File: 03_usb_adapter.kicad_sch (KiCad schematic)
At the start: 5 parts

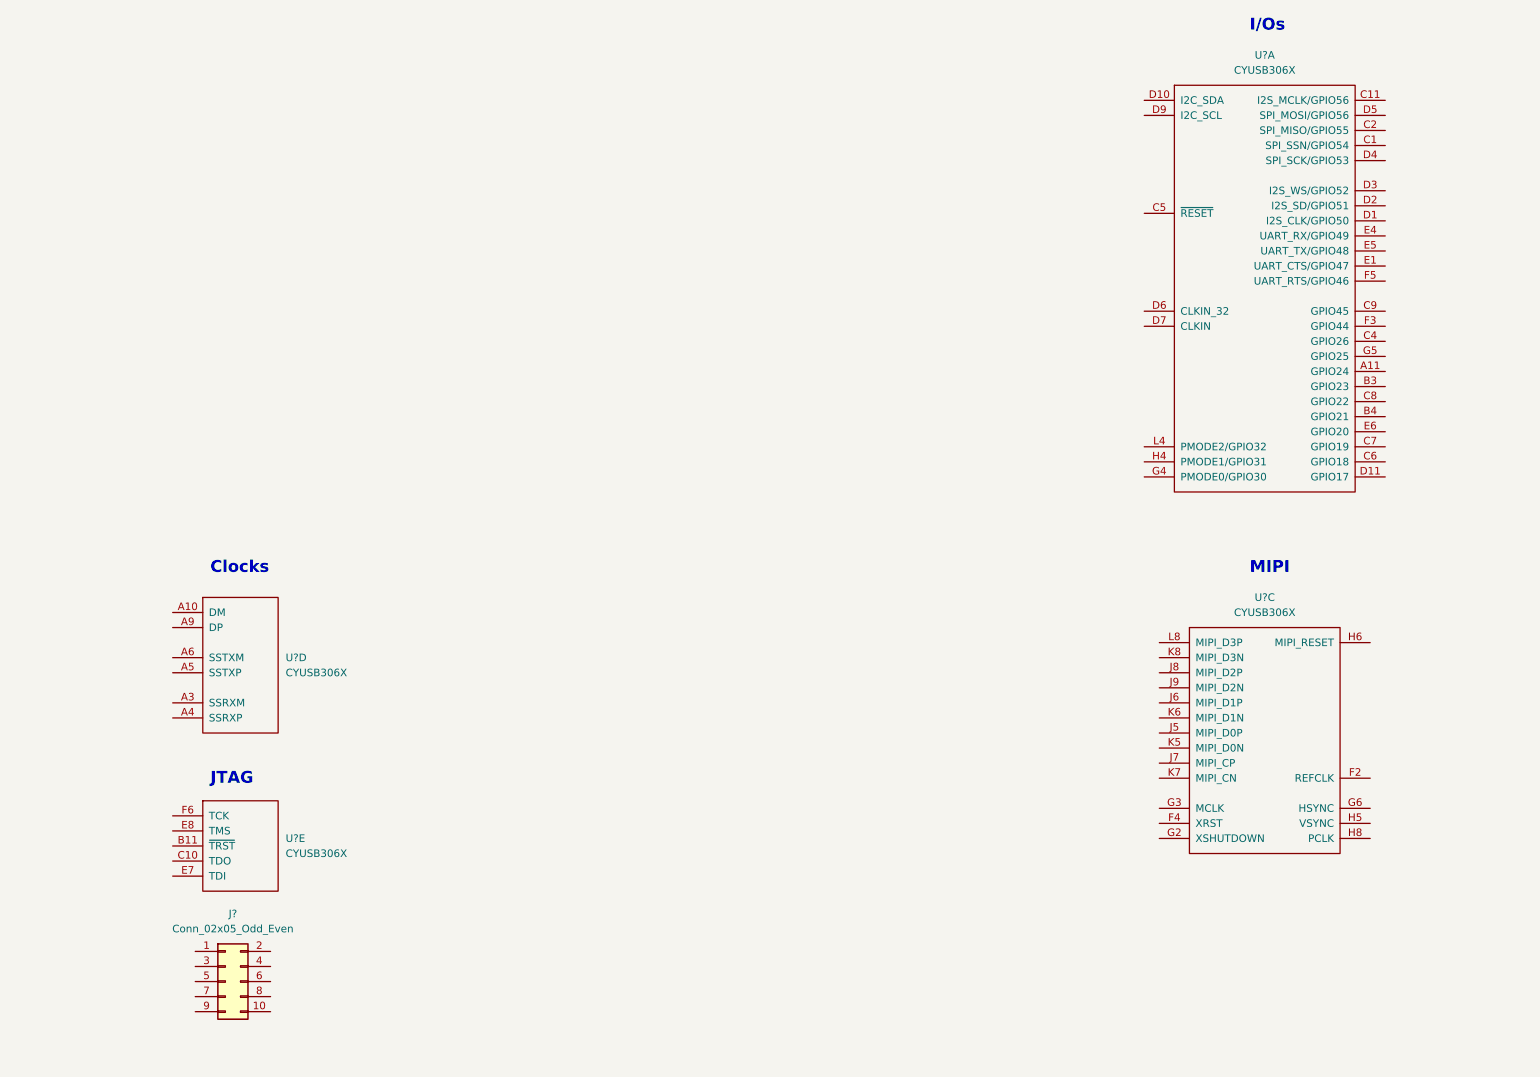
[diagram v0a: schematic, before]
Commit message: finished usb interface and added some new components
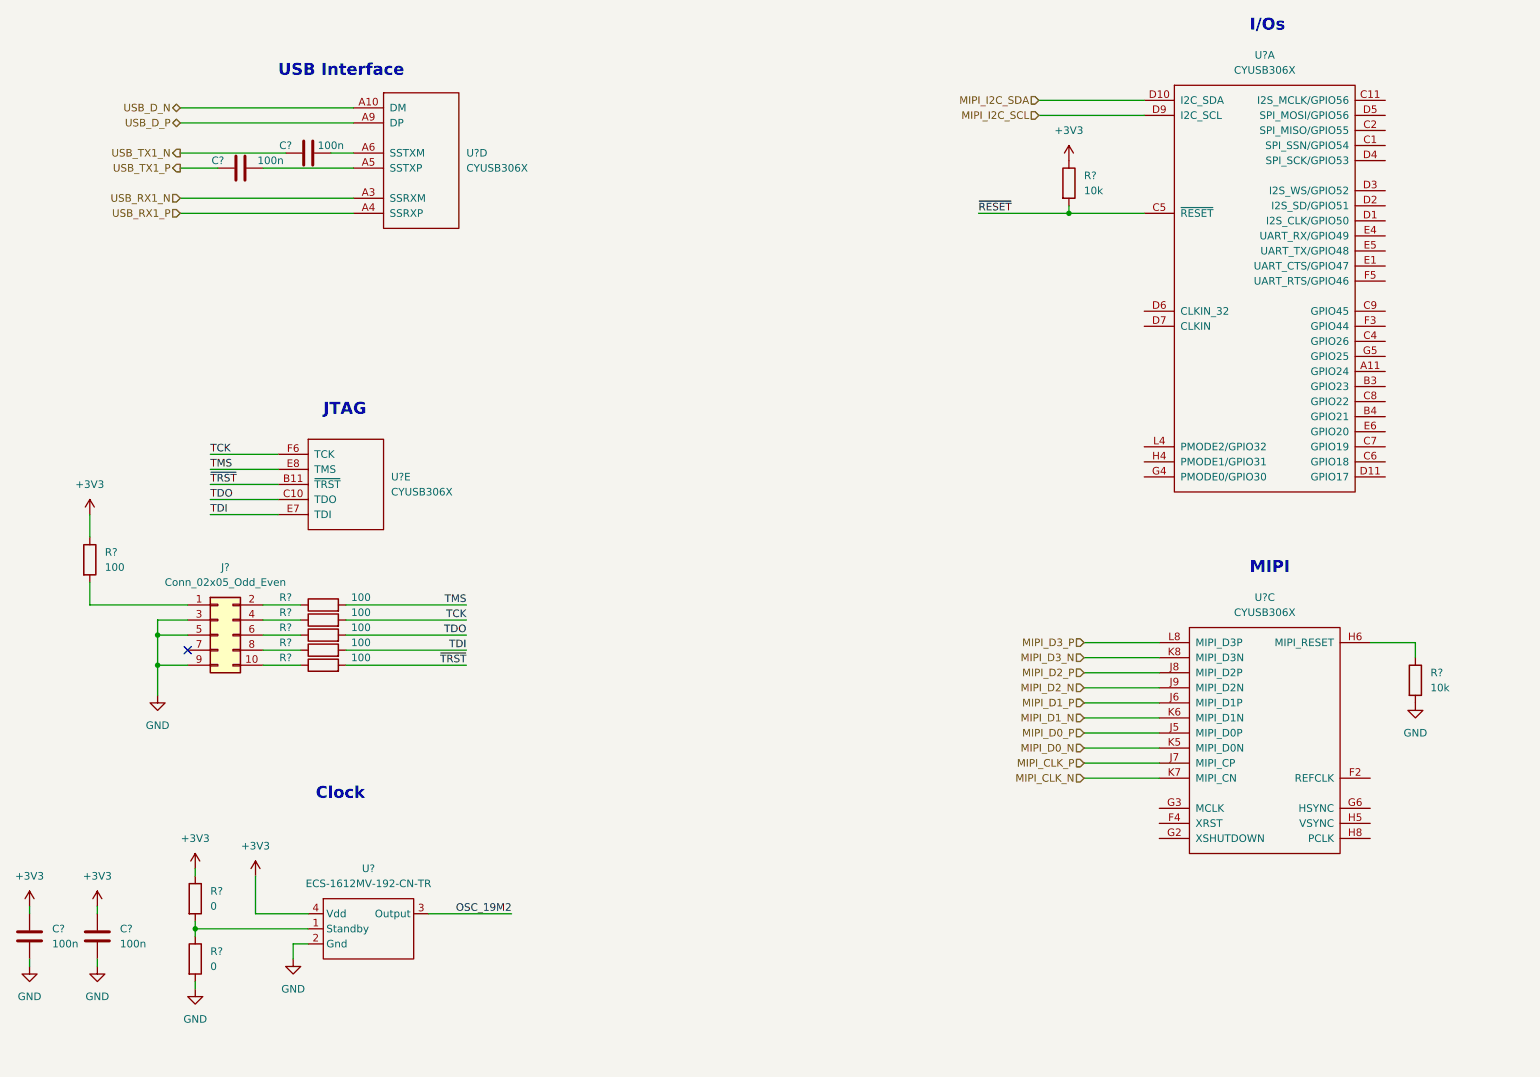
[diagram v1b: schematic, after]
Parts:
- added C? (x2): 100n, Capacitor_SMD:C_0603_1608Metric, symbol Device:C
- added C? (x2): 100n, symbol Device:C
- added R? (x2): 10k, Resistor_SMD:R_0603_1608Metric, symbol Device:R
- added R? (x2): 0, Resistor_SMD:R_0603_1608Metric, symbol Device:R
- added R? (x6): 100, Resistor_SMD:R_0603_1608Metric, symbol Device:R
- added U?: ECS-1612MV-192-CN-TR, samaritan:Crystal_SMD_ECS_1.6x1.2, symbol samaritan:ECS-1612MV-192-CN-TR
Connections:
- net at J?.1 (Pin_1): now also R?.2
- net at J?.10 (Pin_10): now also R?.1
- net at J?.2 (Pin_2): now also R?.1
- net GND: now reaches J?.3 (Pin_3)
- net GND: now also J?.5 (Pin_5), J?.9 (Pin_9), C?.2, C?.2, R?.2, R?.2, U?.2 (Gnd)
- net at J?.4 (Pin_4): now also R?.1
- net at J?.6 (Pin_6): now also R?.1
- net at J?.8 (Pin_8): now also R?.1
- net at U?.H6 (MIPI_RESET): now also R?.1
- net MIPI_D0_P: now reaches U?.J5 (MIPI_D0P)
- net MIPI_D1_P: now reaches U?.J6 (MIPI_D1P)
- net MIPI_CLK_P: now reaches U?.J7 (MIPI_CP)
- net MIPI_D2_P: now reaches U?.J8 (MIPI_D2P)
- net MIPI_D2_N: now reaches U?.J9 (MIPI_D2N)
- net MIPI_D0_N: now reaches U?.K5 (MIPI_D0N)
- net MIPI_D1_N: now reaches U?.K6 (MIPI_D1N)
- net MIPI_CLK_N: now reaches U?.K7 (MIPI_CN)
- net MIPI_D3_N: now reaches U?.K8 (MIPI_D3N)
- net MIPI_D3_P: now reaches U?.L8 (MIPI_D3P)
- net ~{RESET}: now reaches U?.C5 (~{RESET})
- net ~{RESET}: now also R?.2
- net MIPI_I2C_SDA: now reaches U?.D10 (I2C_SDA)
- net MIPI_I2C_SCL: now reaches U?.D9 (I2C_SCL)
- net ~{TRST}: now reaches U?.B11 (~{TRST})
- net ~{TRST}: now also R?.2
- net TDO: now reaches U?.C10 (TDO)
- net TDO: now also R?.2
- net TDI: now reaches U?.E7 (TDI)
- net TDI: now also R?.2
- net TMS: now reaches U?.E8 (TMS)
- net TMS: now also R?.2
- net TCK: now reaches U?.F6 (TCK)
- net TCK: now also R?.2
- net USB_D_N: now reaches U?.A10 (DM)
- net USB_RX1_N: now reaches U?.A3 (SSRXM)
- net USB_RX1_P: now reaches U?.A4 (SSRXP)
- net at U?.A5 (SSTXP): now also C?.2
- net at U?.A6 (SSTXM): now also C?.2
- net USB_D_P: now reaches U?.A9 (DP)
- new net: R?.1, R?.2, U?.1 (Standby)
- new net +3V3: C?.1, C?.1, R?.1, R?.1, R?.1, U?.4 (Vdd)
- new net OSC_19M2: U?.3 (Output)
- new net USB_TX1_N: C?.1
- new net USB_TX1_P: C?.1
- no-connect marks 0 -> 1
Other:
- note added: "Clock"
- note added: "USB Interface"
- note removed: "Clocks"
- moved on the sheet: J?, U?D, U?E

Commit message: added mipi connector
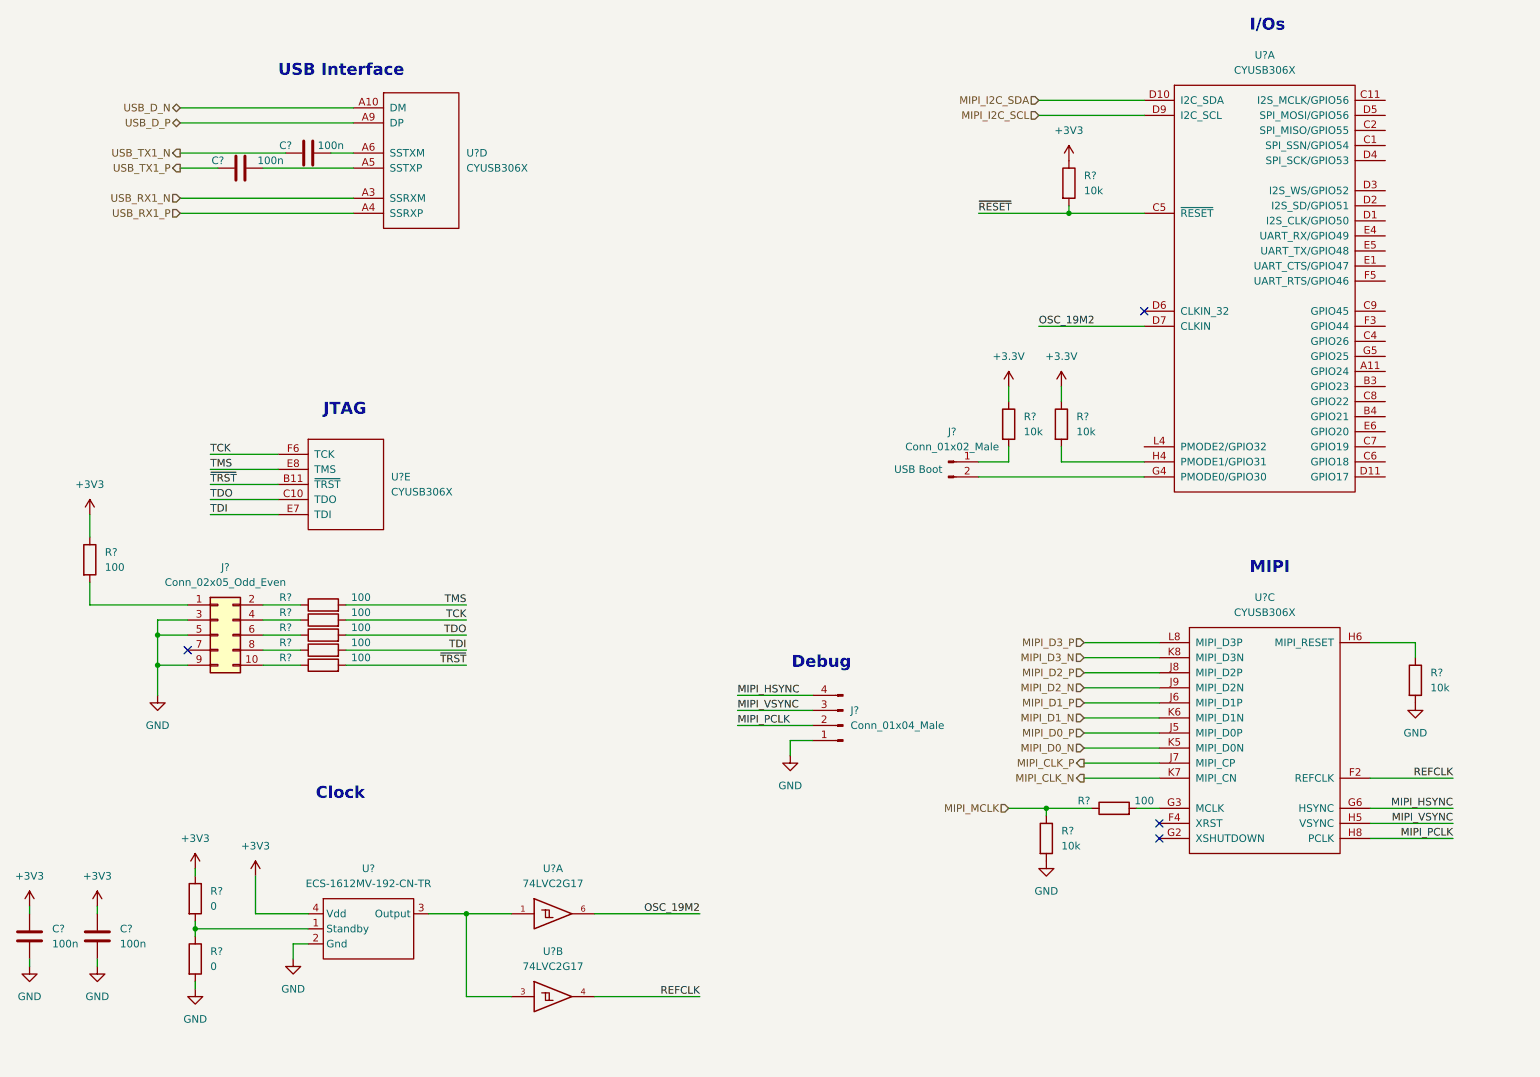
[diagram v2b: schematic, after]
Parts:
- added J?: Conn_01x04_Male, Connector_PinHeader_2.00mm:PinHeader_1x04_P2.00mm_Vertical, symbol Connector:Conn_01x04_Male
- added J?: Conn_01x02_Male, symbol Connector:Conn_01x02_Male
- added R? (x3): 10k, Resistor_SMD:R_0603_1608Metric, symbol Device:R
- added R?: 100, Resistor_SMD:R_0603_1608Metric, symbol Device:R
- added U? (x2): 74LVC2G17, symbol 74xGxx:74LVC2G17
- J?: footprint (none) -> Connector_PinHeader_2.00mm:PinHeader_2x05_P2.00mm_Vertical
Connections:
- net GND: now also J?.1 (Pin_1), R?.2, U?.2 (GND), U?.2 (GND)
- net OSC_19M2: now also U?.D7 (CLKIN), U?.6; no longer U?.3 (Output)
- net REFCLK: now reaches U?.F2 (REFCLK)
- net REFCLK: now also U?.4
- net at U?.G3 (MCLK): now also R?.2
- net MIPI_HSYNC: now reaches U?.G6 (HSYNC)
- net MIPI_HSYNC: now also J?.4 (Pin_4)
- net MIPI_VSYNC: now reaches U?.H5 (VSYNC)
- net MIPI_VSYNC: now also J?.3 (Pin_3)
- net MIPI_PCLK: now reaches U?.H8 (PCLK)
- net MIPI_PCLK: now also J?.2 (Pin_2)
- net at U?.G4 (PMODE0/GPIO30): now also J?.2 (Pin_2)
- net at U?.H4 (PMODE1/GPIO31): now also R?.2
- new net: U?.1, U?.3, U?.3 (Output)
- new net: J?.1 (Pin_1), R?.2
- new net +3.3V: R?.1, R?.1
- new net MIPI_MCLK: R?.1, R?.1
- new net VCC: U?.5 (VCC), U?.5 (VCC)
- no-connect marks 1 -> 4
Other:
- note added: "Debug"

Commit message: finished first pass of the schematics
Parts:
- U?: footprint (none) -> Package_BGA:TFBGA-121_10x10mm_Layout11x11_P0.8mm
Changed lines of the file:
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@@
     (effects (font (size 1.27 1.27)) (justify right))
   )
-  (hierarchical_label "MIPI_I2C_SCL" (shape input) (at 195.58 34.29 180)
+  (hierarchical_label "MIPI_I2C_SCL" (shape output) (at 195.58 34.29 180)
     (effects (font (size 1.27 1.27)) (justify right))
   )
@@
     (effects (font (size 1.27 1.27)) (justify right))
   )
-  (hierarchical_label "MIPI_I2C_SDA" (shape input) (at 195.58 31.75 180)
+  (hierarchical_label "MIPI_I2C_SDA" (shape bidirectional) (at 195.58 31.75 180)
     (effects (font (size 1.27 1.27)) (justify right))
   )
@@
     (effects (font (size 1.27 1.27)) (justify right))
   )
-  (hierarchical_label "MIPI_MCLK" (shape input) (at 190.5 151.13 180)
+  (hierarchical_label "MIPI_MCLK" (shape output) (at 190.5 151.13 180)
     (effects (font (size 1.27 1.27)) (justify right))
   )
@@
     (property "Reference" "U?" (id 0) (at 233.68 24.13 0))
     (property "Value" "CYUSB306X" (id 1) (at 233.68 26.67 0))
-    (property "Footprint" "" (id 2) (at 242.57 92.71 0)
-      (effects (font (size 1.27 1.27)) hide)
-    )
+    (property "Footprint" "Package_BGA:TFBGA-121_10x10mm_Layout11x11_P0.8mm" (id 2) (at 242.57 92.71 0)
+      (effects (font (size 1.27 1.27)) hide)
+    )

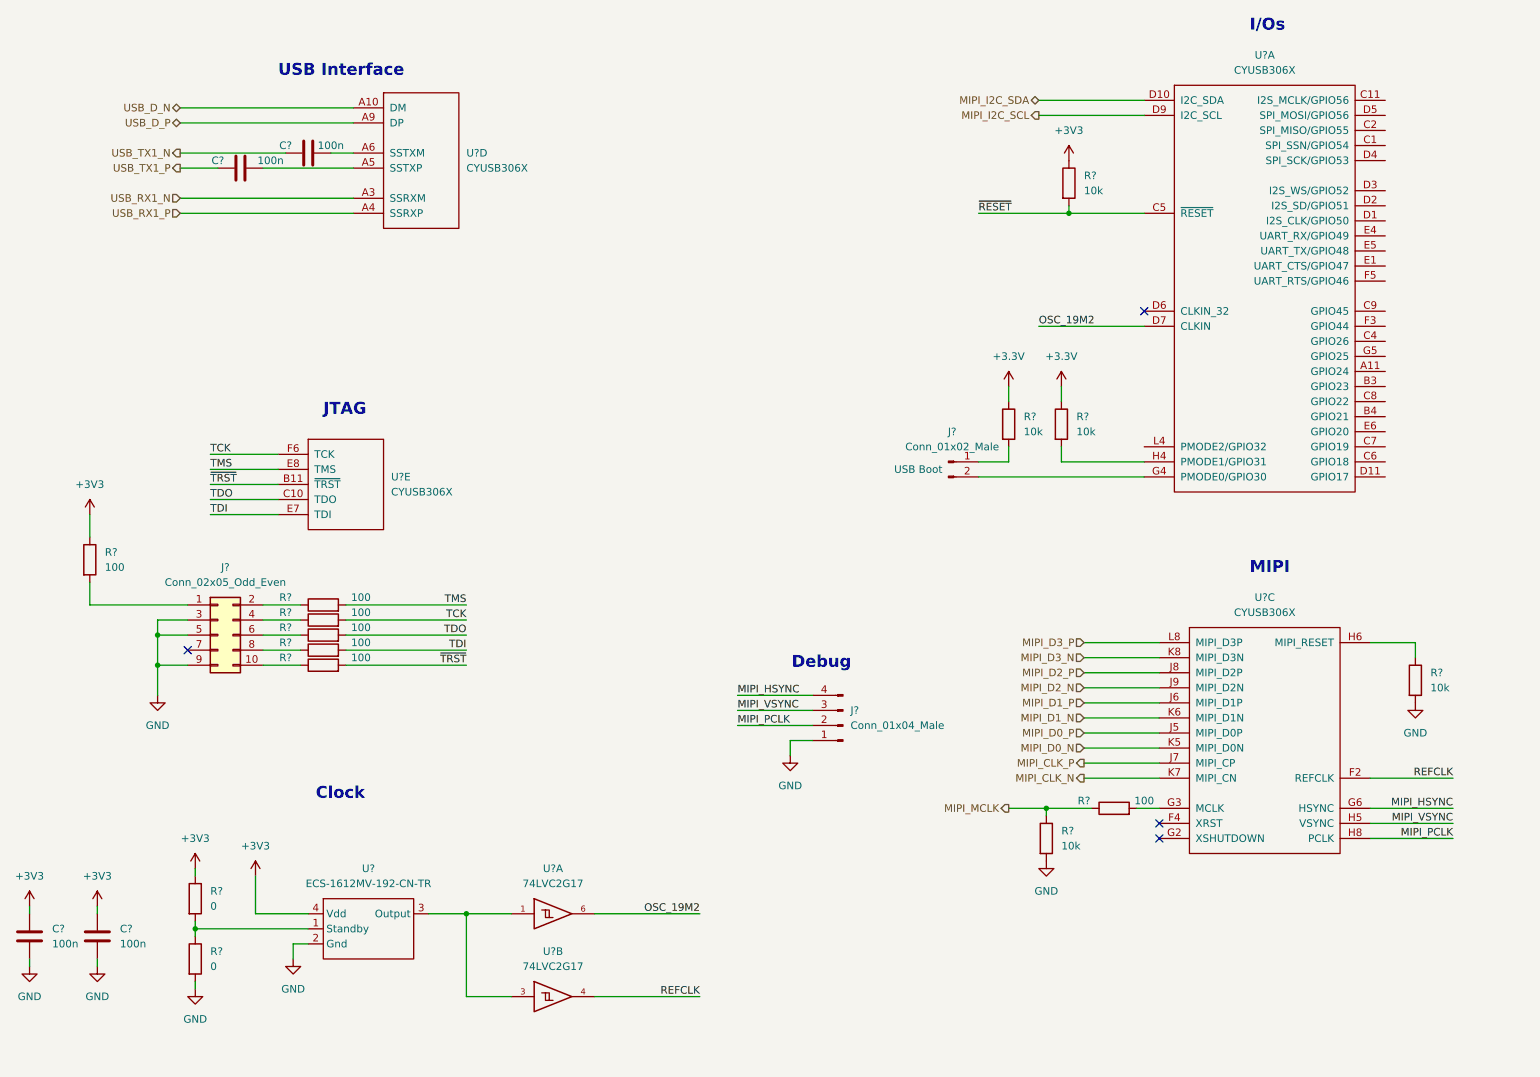
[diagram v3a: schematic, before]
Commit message: cleaned up some DRC errors
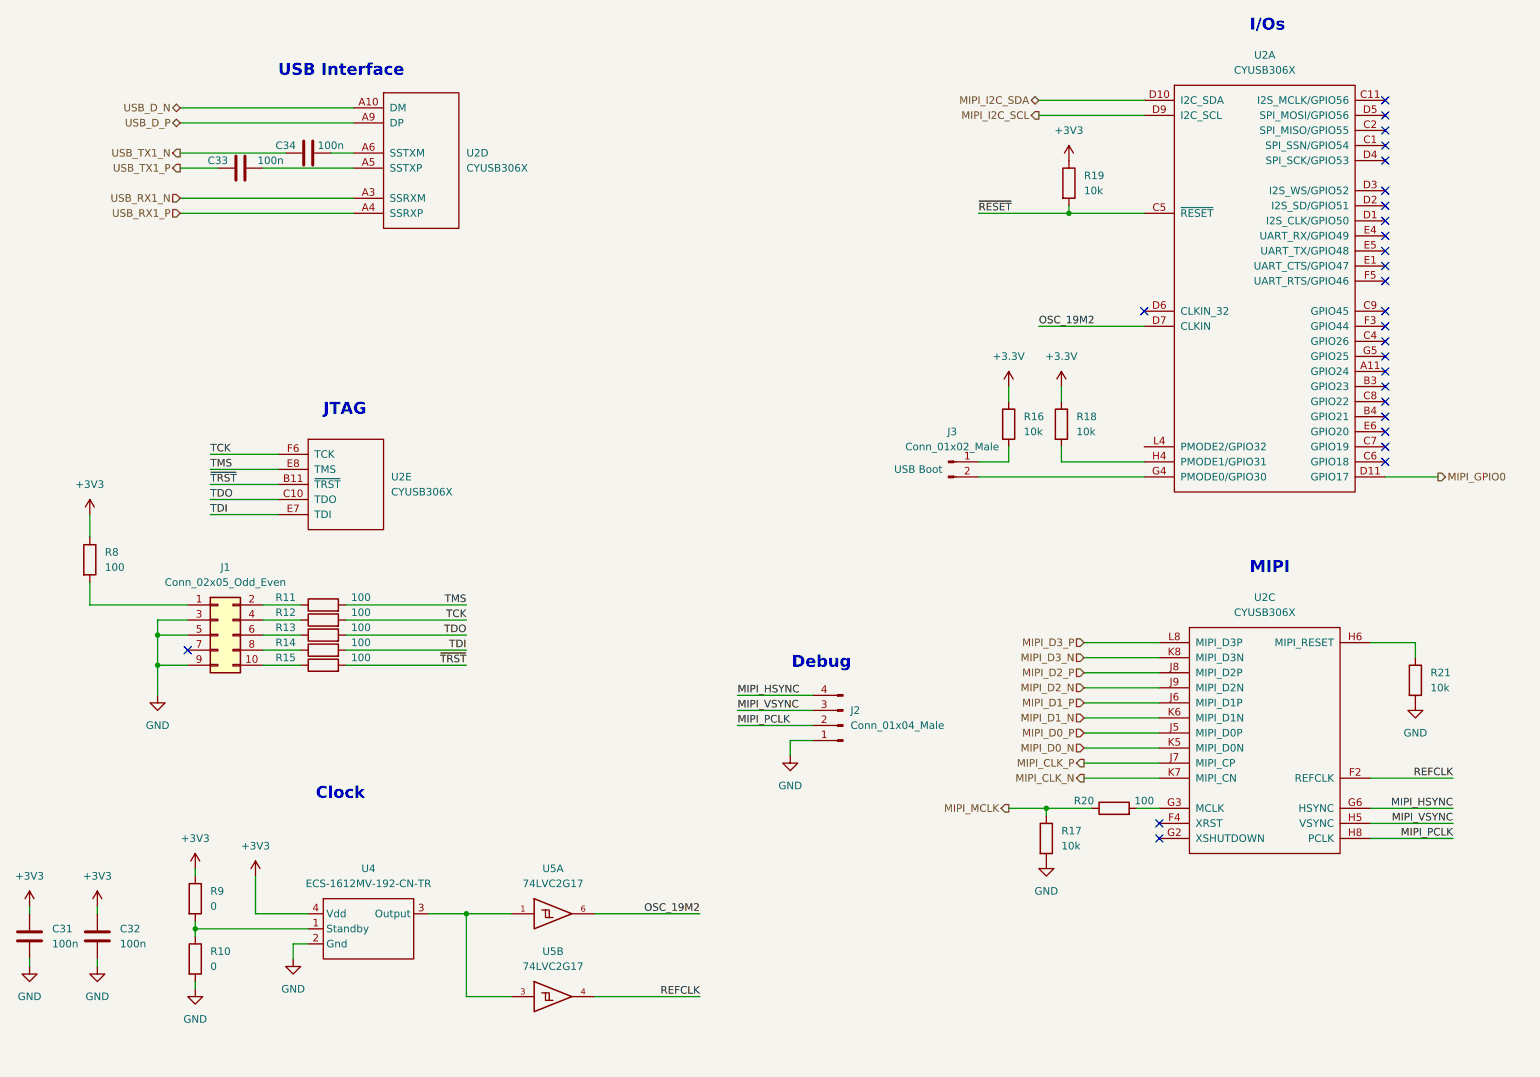
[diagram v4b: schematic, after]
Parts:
- U2: renamed from U?; footprint (none) -> Package_BGA:XBGA-121_10x10mm_Layout11x11_P0.8mm
- U2: renamed from U?; footprint Package_BGA:TFBGA-121_10x10mm_Layout11x11_P0.8mm -> Package_BGA:XBGA-121_10x10mm_Layout11x11_P0.8mm
- U5: renamed from U?; footprint (none) -> Package_TO_SOT_SMD:SOT-363_SC-70-6
- gave numbers to parts that had none: 22
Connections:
- net MIPI_GPIO0: now reaches U2.D11 (GPIO17)
- no-connect marks 4 -> 27
